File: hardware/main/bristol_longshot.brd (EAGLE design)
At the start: 14 x 64 mm, 72 parts, among them U1 SAM_D20E, U2 SI4060, U3 SN74LVC1G32DCKR, U4 AD8354, U5 S25FS-S, Y1 ABS05

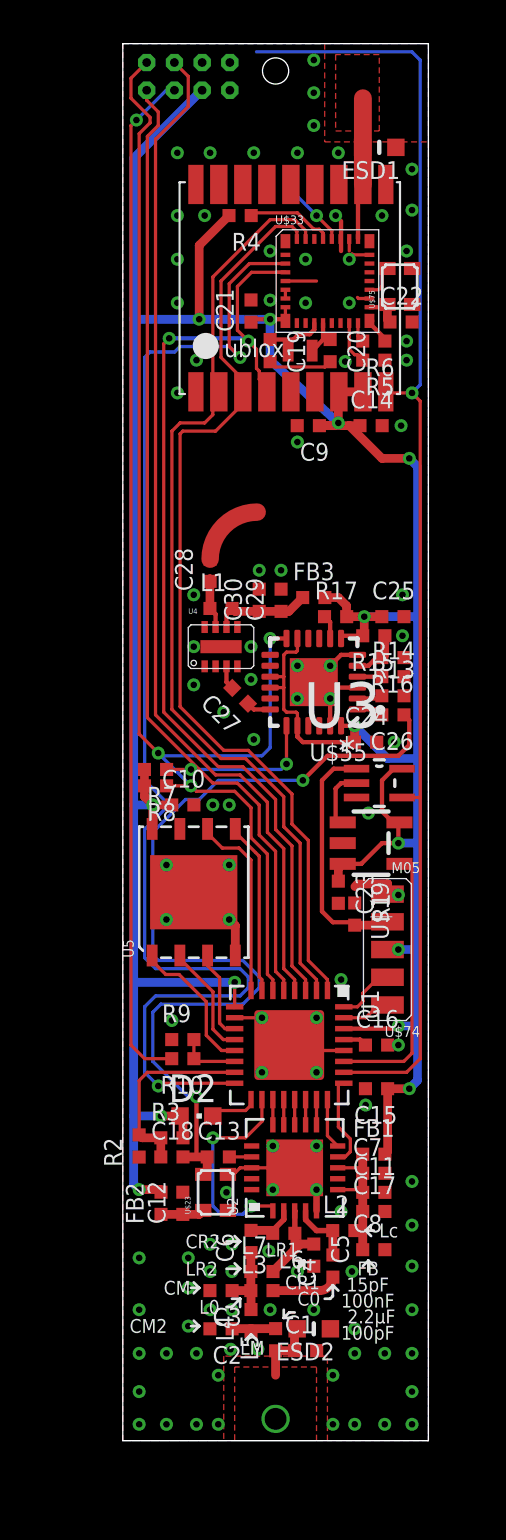
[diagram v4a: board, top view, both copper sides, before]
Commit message: Actually update main board to v0.98.0
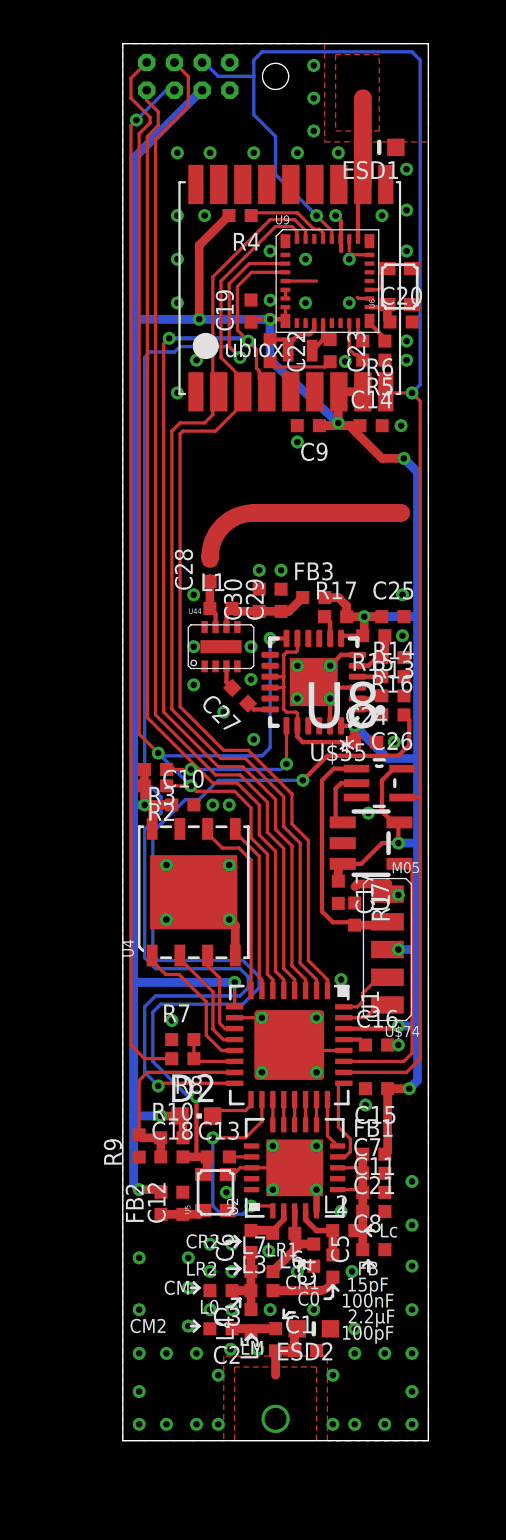
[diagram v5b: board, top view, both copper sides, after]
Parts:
- removed U$23: TG-5006CJ, fbri:TC-5006CJ
- removed U$48: UBLOX_MAX, Ava:UBLOX_MAX
- added U44: AD8354, fbri:LFCSP_VD_8
- added U8: SN74LVC1G32DCKR, SN74LVC1G32DCKR:SOT65P210X110-5N
- C17: value 2.2µF -> 100nF
- C19, C20: value 18pF -> 100nF
- C21: value 100nF -> 2.2µF
- C22, C23: value 100nF -> 18pF
- R10: value 22kΩ -> 100kΩ
- R2, R3: value 100kΩ -> 10kΩ
- R8: value 10kΩ -> 22kΩ
- R9: value 10kΩ -> 100kΩ
- U3: value SN74LVC1G32DCKR -> UBLOX_MAX; device SN74LVC1G32DCKR:SOT65P210X110-5N -> Ava:UBLOX_MAX
- U4: value AD8354 -> S25FS-S; device fbri:LFCSP_VD_8 -> fbri:WSON8
- U5: value S25FS-S -> TG-5006CJ; device fbri:WSON8 -> fbri:TC-5006CJ
- moved C21 41.6 mm to (11.5, 10.5), turned to 0 degrees
- moved C23 24.8 mm to (9.50, 49.9)
- moved U3 23.2 mm to (7.75, 53.0), turned to 270 degrees
- moved R3 16.9 mm to (1.50, 30.8), turned to 180 degrees
- moved R2 16.5 mm to (1.50, 30.0), turned to 180 degrees
- moved C17 14.7 mm to (9.88, 25.1), turned to 270 degrees
- moved U5 13.8 mm to (4.25, 11.4)
- moved R8 12.6 mm to (2.75, 17.5)
- moved R7 12.4 mm to (2.75, 18.4), turned to 0 degrees
- moved U4 11.3 mm to (3.25, 25.1), turned to 90 degrees
- moved C22 6.14 mm to (6.75, 49.9), turned to 270 degrees
- moved R9 5.27 mm to (0.75, 13.5), turned to 90 degrees
- moved R10 3.66 mm to (2.25, 13.9), turned to 0 degrees
- moved C20 3.51 mm to (12.8, 51.2), turned to 0 degrees
- moved C19 2.01 mm to (5.88, 51.8), turned to 90 degrees
- renumbered U$19 to U7, U$33 to U9, U$75 to U6
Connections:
- net HF renamed HF_ANT
- net !RESET: now also U3.9_V_RESET, U8.4; no longer U$48.9_V_RESET, U3.4
- net 1.2V: now also R8.2; no longer R10.2
- net 1.8V: now also C17.1, C19.1, R10.2, R2.2, U3.7_VCC_IO, U3.8_VCC, U4.8, U8.5; no longer C21.1, C23.1, R7.2, R8.2, U$48.7_VCC_IO, U$48.8_VCC, U3.5, U5.8
- net AMPL_OUT: now also U44.7; no longer U4.7
- net AMPL_VPOS: now also U44.6; no longer U4.6
- net EXT!RESET: now also U8.1; no longer U3.1
- net GIMO: now also U3.3_RXD1; no longer U$48.3_RXD1
- net GND: now also R7.1, U3.10_GND, U3.12_GND, U3.1_GND, U4.PAD, U44.1, U44.4, U44.5, U44.8, U44.EPAD, U5.2, U8.3; no longer R2.1, U$23.2, U$48.10_GND, U$48.12_GND, U$48.1_GND, U3.3, U4.1, U4.5, U4.8, U4.EPAD, U5.4, U5.PAD
- net GOMI: now also U3.2_TXD1; no longer U$48.2_TXD1
- net GPS_ANT: now also U3.11_RF_IN; no longer U$48.11_RF_IN
- net INPT: now also U44.3; no longer U4.3
- net MEM_CSN: now also U4.1; no longer U5.1
- net MEM_MISO: now also U4.2; no longer U5.2
- net MEM_MOSI: now also U4.5; no longer U5.5
- net MEM_SCK: now also U4.6; no longer U5.6
- net MEM_WPN: now also U4.3; no longer U5.3
- net RADIO_VDD: now also C21.1; no longer C17.1
- net RTC_XI: now also C22.1; no longer C19.1
- net RTC_XO: now also C23.1; no longer C20.1
- net SAM_XOSC: now also R10.1, R9.2; no longer R2.2, R3.1
- net SCL: now also R2.1; no longer R8.1
- net SDA: now also R3.1; no longer R7.1
- net SE_VCO_TCXO: now also C20.1; no longer C22.1
- net TCXO_OUT: now also U5.3; no longer U$23.3
- net TCXO_VDD: now also U5.4; no longer U$23.4
- net TIMEPULSE: now also U3.4_TIMEPULSE; no longer U$48.4_TIMEPULSE
- net VBATT_SENSE: now also R7.2, R8.1; no longer R10.1, R9.2
- net WDI!RESET: now also U8.2; no longer U3.2
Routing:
- net HF_ANT: track 3.05 -> 16.4 mm
- net !RESET: track 62.7 -> 72.1 mm
- net 1.8V: track 165.7 -> 166.2 mm
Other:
- board text added: "V0.98.0"
- board text removed: "OF"
- board text removed: "v0.96.0"
